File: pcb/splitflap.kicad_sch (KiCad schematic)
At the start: 61 parts, among them J1 Conn_01x05, J10 Hall C, J11 Hall-D, J12 I2C, J2 Conn_01x05, J3 Conn_01x05, J4 Conn_01x05, J5 Barrel_Jack_Switch, J6 USB_C_Receptacle_USB2.0_16P, J7 Barrel_Jack_Switch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

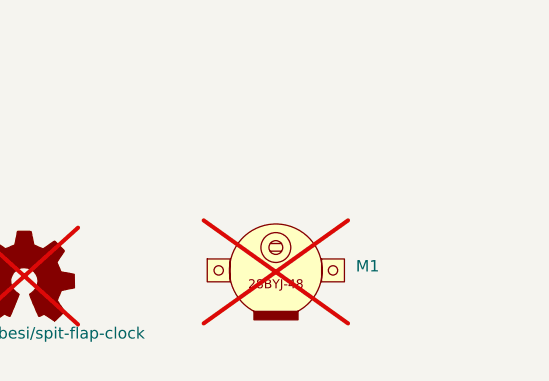
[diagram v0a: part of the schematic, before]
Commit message: Silkscreen improvements
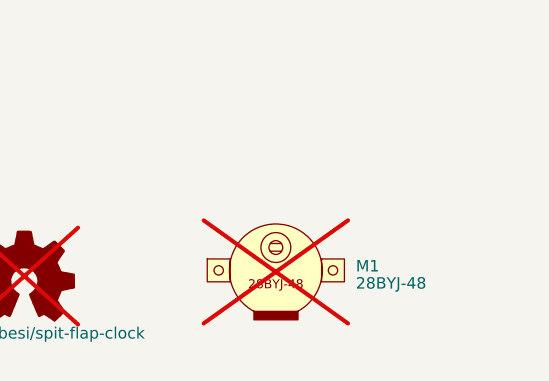
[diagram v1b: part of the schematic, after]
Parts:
- M1: value ~ -> 28BYJ-48
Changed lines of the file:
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@@
 			)
 		)
-		(property "Value" "~"
+		(property "Value" "28BYJ-48"
 			(at 269.24 174.1571 0)
 			(effects

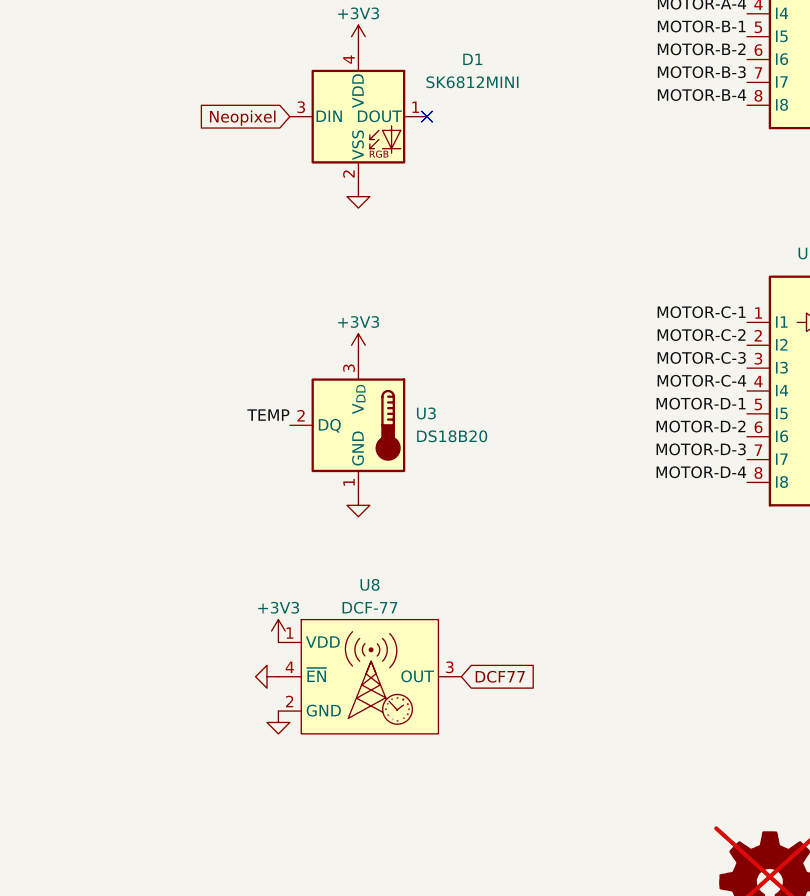
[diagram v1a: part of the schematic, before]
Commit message: Add optional LED for DCF receiver
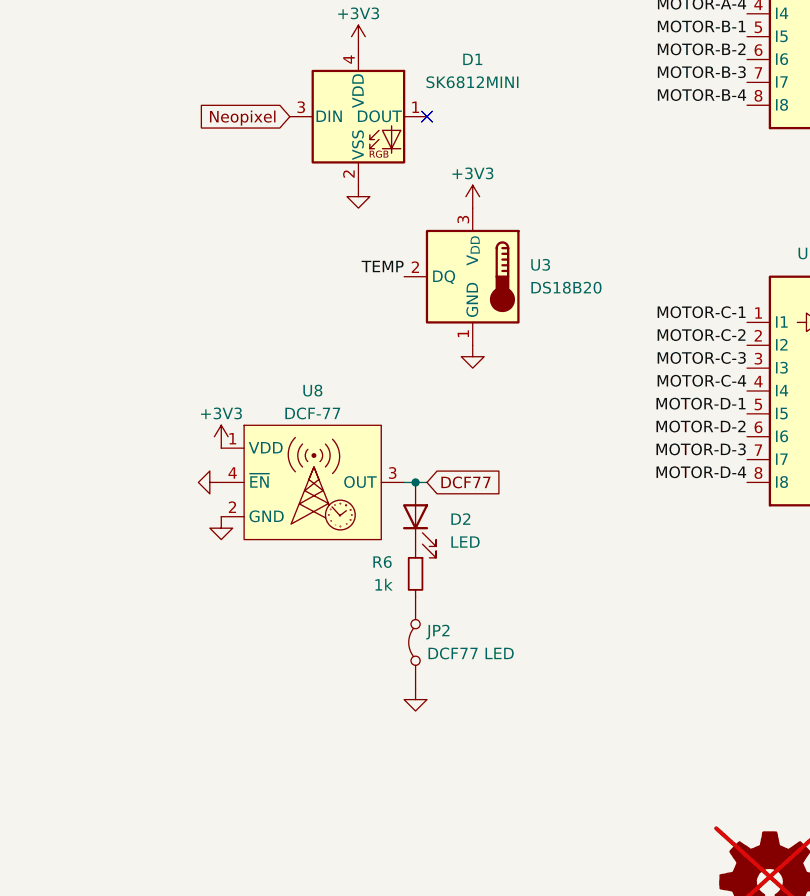
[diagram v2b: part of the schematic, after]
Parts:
- added D2: LED, LED_SMD:LED_0603_1608Metric_Pad1.05x0.95mm_HandSolder, symbol Device:LED
- added JP2: DCF77 LED, Jumper:SolderJumper-2_P1.3mm_Bridged_RoundedPad1.0x1.5mm, symbol Jumper:Jumper_2_Bridged
- added R6: 1k, Resistor_SMD:R_0603_1608Metric, symbol Device:R_Small
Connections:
- net DCF77: now also D2.2 (A)
- net GND: now also JP2.1 (A)
- new net: D2.1 (K), R6.1
- new net: JP2.2 (B), R6.2
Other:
- moved on the sheet: U3, U8

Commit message: Add two Hall sensors to the current board so that the amount of backlash can be registered
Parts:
- removed JP1: Hall-A Switch, Jumper:SolderJumper-3_P1.3mm_Open_RoundedPad1.0x1.5mm, symbol Jumper:Jumper_3_Bridged12
- removed TP1: IO7, TestPoint:TestPoint_Pad_D1.5mm, symbol Connector:TestPoint
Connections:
- net Extra is gone; now on net HALL_A2: U4.7 (IO7)
- net HALL_A is gone; now on net HALL_A1: J8.2 (Pin_2), U4.11 (IO18)
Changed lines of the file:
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@@
 		)
 	)
-	(label "HALL_A"
+	(label "HALL_A1"
 		(at 34.29 77.47 0)
 		(effects
@@
 	)
 	(label "HALL_A1"
-		(at 158.75 19.05 180)
+		(at 133.35 129.54 0)
 		(effects
 			(font
 				(size 1.27 1.27)
 			)
-			(justify right bottom)
+			(justify left bottom)
 		)
 	)
@@
 	)
 	(label "HALL_A2"
-		(at 171.45 19.05 0)
+		(at 133.35 101.6 0)
 		(effects
 			(font
@@
 		)
 	)
-	(label "HALL_A"
-		(at 165.1 22.86 270)
-		(effects
-			(font
-				(size 1.27 1.27)
-			)
-			(justify right bottom)
-		)
-	)
 	(label "SWA_SCL"
 		(at 133.35 127 0)
@@
 		)
 	)
-	(label "HALL_A"
-		(at 133.35 129.54 0)
-		(effects
-			(font
-				(size 1.27 1.27)
-			)
-			(justify left bottom)
-		)
-	)
 	(label "MOUT-A3"
 		(at 267.97 74.93 180)
@@
 		)
 	)
-	(global_label "Extra"
-		(shape input)
-		(at 133.35 101.6 0)
-		(fields_autoplaced yes)
-		(effects
-			(font
-				(size 1.27 1.27)
-			)
-			(justify left)
-		)
-		(property "Intersheetrefs" "${INTERSHEET_REFS}"
-			(at 141.1732 101.6 0)
-			(effects
-				(font
-					(size 1.27 1.27)
-				)
-				(justify left)
-				(hide yes)
-			)
-		)
-	)
 	(global_label "Neopixel"
 		(shape input)
@@
 		)
 	)
-	(global_label "Extra"
-		(shape input)
-		(at 175.26 67.31 180)
-		(fields_autoplaced yes)
-		(effects
-			(font
-				(size 1.27 1.27)
-			)
-			(justify right)
-		)
-		(property "Intersheetrefs" "${INTERSHEET_REFS}"
-			(at 167.4368 67.31 0)
-			(effects
-				(font
-					(size 1.27 1.27)
-				)
-				(justify right)
-				(hide yes)
-			)
-		)
-	)
 	(global_label "DCF77"
 		(shape input)
@@
 	)
 	(symbol
-		(lib_id "Jumper:Jumper_3_Bridged12")
-		(at 165.1 19.05 0)
-		(unit 1)
-		(exclude_from_sim yes)
-		(in_bom no)
-		(on_board yes)
-		(dnp no)
-		(fields_autoplaced yes)
-		(property "Reference" "JP1"
-			(at 165.1 12.7 0)
-			(effects
-				(font
-					(size 1.27 1.27)
-				)
-			)
-		)
-		(property "Value" "Hall-A Switch"
-			(at 165.1 15.24 0)
-			(effects
-				(font
-					(size 1.27 1.27)
-				)
-			)
-		)
-		(property "Footprint" "Jumper:SolderJumper-3_P1.3mm_Open_RoundedPad1.0x1.5mm"
-			(at 165.1 19.05 0)
-			(effects
-				(font
-					(size 1.27 1.27)
-				)
-				(hide yes)
-			)
-		)
-		(property "Datasheet" "~"
-			(at 165.1 19.05 0)
-			(effects
-				(font
-					(size 1.27 1.27)
-				)
-				(hide yes)
-			)
-		)
-		(property "Description" "Jumper, 3-pole, pins 1+2 closed/bridged"
-			(at 165.1 19.05 0)
-			(effects
-				(font
-					(size 1.27 1.27)
-				)
-				(hide yes)
-			)
-		)
-		(pin "1"
-		)
-		(pin "3"
-		)
-		(pin "2"
-		)
-		(instances
-			(project ""
-				(path "/f3b5a3df-7272-4af1-9be6-6c38555ab067"
-					(reference "JP1")
-					(unit 1)
-				)
-			)
-		)
-	)
-	(symbol
 		(lib_id "power:GND")
 		(at 36.83 97.79 0)
@@
 					(unit 1)
 				)
-			)
-		)
-	)
-	(symbol
-		(lib_id "Connector:TestPoint")
-		(at 175.26 67.31 270)
-		(unit 1)
-		(exclude_from_sim no)
-		(in_bom yes)
-		(on_board yes)
-		(dnp no)
-		(fields_autoplaced yes)
-		(property "Reference" "TP1"
-			(at 180.34 66.0399 90)
-			(effects
-				(font
-					(size 1.27 1.27)
-				)
-				(justify left)
-			)
-		)
-		(property "Value" "IO7"
-			(at 180.34 68.5799 90)
-			(effects
-				(font
-					(size 1.27 1.27)
-				)
-				(justify left)
-			)
-		)
-		(property "Footprint" "TestPoint:TestPoint_Pad_D1.5mm"
-			(at 175.26 72.39 0)
-			(effects
-				(font
-					(size 1.27 1.27)
-				)
-				(hide yes)
-			)
-		)
-		(property "Datasheet" "~"
-			(at 175.26 72.39 0)
-			(effects
-				(font
-					(size 1.27 1.27)
-				)
-				(hide yes)
-			)
-		)
-		(property "Description" "test point"
-			(at 175.26 67.31 0)
-			(effects
-				(font
-					(size 1.27 1.27)
-				)
-				(hide yes)
-			)
-		)
-		(pin "1"
-		)
-		(instances
-			(project ""
-				(path "/f3b5a3df-7272-4af1-9be6-6c38555ab067"
-					(reference "TP1")
-					(unit 1)
-				)

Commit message: Remapping the motors ABCD to match the connectors on the board
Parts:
- J1: value Conn_01x05 -> Motor D
- J11: value Hall-D -> Hall B
- J2: value Conn_01x05 -> Motor C
- J3: value Conn_01x05 -> Motor B
- J4: value Conn_01x05 -> Motor A
- J8: value Hall A -> Hall A1
- J9: value Hall B -> Hall D
- U5: value AH1815-W-7 -> Hall A1; MPN (none) -> AH1815-W-7
- U9: value AH1815-W-7 -> Hall A2; MPN (none) -> AH1815-W-7
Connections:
- net HALL_B: now also J11.2 (Pin_2), U4.20 (IO12); no longer J9.2 (Pin_2), U4.25 (IO48)
- net HALL_D: now also J9.2 (Pin_2), U4.25 (IO48); no longer J11.2 (Pin_2), U4.20 (IO12)
- net MOTOR-A-1: now also U2.5 (I5), U4.18 (IO10); no longer U1.1 (I1), U4.39 (IO1)
- net MOTOR-A-2: now also U2.6 (I6), U4.17 (IO9); no longer U1.2 (I2), U4.38 (IO2)
- net MOTOR-A-3: now also U2.7 (I7), U4.15 (IO3); no longer U1.3 (I3), U4.35 (MTMS/IO42)
- net MOTOR-A-4: now also U2.8 (I8), U4.12 (IO8); no longer U1.4 (I4), U4.34 (MTDI/IO41)
- net MOTOR-B-1: now also U2.1 (I1), U4.21 (IO13); no longer U1.5 (I5), U4.33 (MTDO/IO40)
- net MOTOR-B-2: now also U2.2 (I2), U4.22 (IO14); no longer U1.6 (I6), U4.32 (MTCK/IO39)
- net MOTOR-B-3: now also U2.3 (I3), U4.23 (IO21); no longer U1.7 (I7), U4.31 (IO38)
- net MOTOR-B-4: now also U2.4 (I4), U4.19 (IO11); no longer U1.8 (I8), U4.6 (IO6)
- net MOTOR-C-1: now also U1.5 (I5), U4.33 (MTDO/IO40); no longer U2.1 (I1), U4.21 (IO13)
- net MOTOR-C-2: now also U1.6 (I6), U4.32 (MTCK/IO39); no longer U2.2 (I2), U4.22 (IO14)
- net MOTOR-C-3: now also U1.7 (I7), U4.31 (IO38); no longer U2.3 (I3), U4.23 (IO21)
- net MOTOR-C-4: now also U1.8 (I8), U4.6 (IO6); no longer U2.4 (I4), U4.19 (IO11)
- net MOTOR-D-1: now also U1.1 (I1), U4.39 (IO1); no longer U2.5 (I5), U4.18 (IO10)
- net MOTOR-D-2: now also U1.2 (I2), U4.38 (IO2); no longer U2.6 (I6), U4.17 (IO9)
- net MOTOR-D-3: now also U1.3 (I3), U4.35 (MTMS/IO42); no longer U2.7 (I7), U4.15 (IO3)
- net MOTOR-D-4: now also U1.4 (I4), U4.34 (MTDI/IO41); no longer U2.8 (I8), U4.12 (IO8)
- net MOUT-A1: now also J4.1 (Pin_1), U2.14 (O5); no longer J1.1 (Pin_1), U1.18 (O1)
- net MOUT-A2: now also J4.2 (Pin_2), U2.13 (O6); no longer J1.2 (Pin_2), U1.17 (O2)
- net MOUT-A3: now also J4.3 (Pin_3), U2.12 (O7); no longer J1.3 (Pin_3), U1.16 (O3)
- net MOUT-A4: now also J4.4 (Pin_4), U2.11 (O8); no longer J1.4 (Pin_4), U1.15 (O4)
- net MOUT-B1: now also J3.1 (Pin_1), U2.18 (O1); no longer J2.1 (Pin_1), U1.14 (O5)
- net MOUT-B2: now also J3.2 (Pin_2), U2.17 (O2); no longer J2.2 (Pin_2), U1.13 (O6)
- net MOUT-B3: now also J3.3 (Pin_3), U2.16 (O3); no longer J2.3 (Pin_3), U1.12 (O7)
- net MOUT-B4: now also J3.4 (Pin_4), U2.15 (O4); no longer J2.4 (Pin_4), U1.11 (O8)
- net MOUT-C1: now also J2.1 (Pin_1), U1.14 (O5); no longer J3.1 (Pin_1), U2.18 (O1)
- net MOUT-C2: now also J2.2 (Pin_2), U1.13 (O6); no longer J3.2 (Pin_2), U2.17 (O2)
- net MOUT-C3: now also J2.3 (Pin_3), U1.12 (O7); no longer J3.3 (Pin_3), U2.16 (O3)
- net MOUT-C4: now also J2.4 (Pin_4), U1.11 (O8); no longer J3.4 (Pin_4), U2.15 (O4)
- net MOUT-D1: now also J1.1 (Pin_1), U1.18 (O1); no longer J4.1 (Pin_1), U2.14 (O5)
- net MOUT-D2: now also J1.2 (Pin_2), U1.17 (O2); no longer J4.2 (Pin_2), U2.13 (O6)
- net MOUT-D3: now also J1.3 (Pin_3), U1.16 (O3); no longer J4.3 (Pin_3), U2.12 (O7)
- net MOUT-D4: now also J1.4 (Pin_4), U1.15 (O4); no longer J4.4 (Pin_4), U2.11 (O8)
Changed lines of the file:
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@@
 		)
 	)
-	(label "MOTOR-B-1"
+	(label "MOTOR-C-1"
 		(at 229.87 80.01 180)
 		(effects
@@
 	)
 	(label "MOUT-B3"
-		(at 267.97 88.9 180)
+		(at 267.97 116.84 180)
 		(effects
 			(font
@@
 		)
 	)
-	(label "MOUT-A2"
+	(label "MOUT-D2"
 		(at 267.97 72.39 180)
 		(effects
@@
 		)
 	)
-	(label "MOTOR-B-2"
+	(label "MOTOR-C-2"
 		(at 229.87 82.55 180)
 		(effects
@@
 		)
 	)
-	(label "MOTOR-B-1"
+	(label "MOTOR-C-1"
 		(at 133.35 144.78 0)
 		(effects
@@
 		)
 	)
-	(label "MOTOR-D-2"
+	(label "MOTOR-A-2"
 		(at 229.87 124.46 180)
 		(effects
@@
 		)
 	)
-	(label "MOTOR-C-3"
+	(label "MOTOR-B-3"
 		(at 133.35 137.16 0)
 		(effects
@@
 		)
 	)
-	(label "MOTOR-D-1"
+	(label "MOTOR-A-1"
 		(at 229.87 121.92 180)
 		(effects
@@
 		)
 	)
-	(label "MOTOR-D-3"
+	(label "MOTOR-A-3"
 		(at 229.87 127 180)
 		(effects
@@
 		)
 	)
-	(label "MOTOR-D-1"
+	(label "MOTOR-A-1"
 		(at 133.35 109.22 0)
 		(effects
@@
 		)
 	)
-	(label "MOTOR-B-4"
+	(label "MOTOR-C-4"
 		(at 133.35 99.06 0)
 		(effects
@@
 		)
 	)
-	(label "MOTOR-B-4"
+	(label "MOTOR-C-4"
 		(at 229.87 87.63 180)
 		(effects
@@
 		)
 	)
-	(label "MOTOR-D-2"
+	(label "MOTOR-A-2"
 		(at 133.35 106.68 0)
 		(effects
@@
 	)
 	(label "MOUT-B2"
-		(at 267.97 86.36 180)
+		(at 267.97 114.3 180)
 		(effects
 			(font
@@
 		)
 	)
-	(label "MOTOR-A-2"
+	(label "MOTOR-D-2"
 		(at 229.87 72.39 180)
 		(effects
@@
 		)
 	)
-	(label "MOUT-A1"
+	(label "MOUT-D1"
 		(at 267.97 69.85 180)
 		(effects
@@
 		)
 	)
-	(label "MOTOR-B-3"
+	(label "MOTOR-C-3"
 		(at 133.35 139.7 0)
 		(effects
@@
 		)
 	)
-	(label "MOTOR-A-3"
+	(label "MOTOR-D-3"
 		(at 229.87 74.93 180)
 		(effects
@@
 		)
 	)
-	(label "MOTOR-A-1"
+	(label "MOTOR-D-1"
 		(at 133.35 86.36 0)
 		(effects
@@
 	)
 	(label "MOUT-C3"
-		(at 267.97 116.84 180)
+		(at 267.97 88.9 180)
 		(effects
 			(font
@@
 		)
 	)
-	(label "MOTOR-B-3"
+	(label "MOTOR-C-3"
 		(at 229.87 85.09 180)
 		(effects
@@
 	)
 	(label "MOUT-B1"
-		(at 267.97 83.82 180)
+		(at 267.97 111.76 180)
 		(effects
 			(font
@@
 		)
 	)
-	(label "MOUT-A4"
+	(label "MOUT-D4"
 		(at 267.97 77.47 180)
 		(effects
@@
 		)
 	)
-	(label "HALL_B"
+	(label "HALL_D"
 		(at 34.29 95.25 0)
 		(effects
@@
 		)
 	)
-	(label "MOTOR-C-3"
+	(label "MOTOR-B-3"
 		(at 229.87 116.84 180)
 		(effects
@@
 		)
 	)
-	(label "MOTOR-C-2"
+	(label "MOTOR-B-2"
 		(at 133.35 119.38 0)
 		(effects
@@
 		)
 	)
-	(label "MOTOR-C-1"
+	(label "MOTOR-B-1"
 		(at 229.87 111.76 180)
 		(effects
@@
 		)
 	)
-	(label "HALL_D"
+	(label "HALL_B"
 		(at 133.35 114.3 0)
 		(effects
@@
 		)
 	)
-	(label "MOTOR-C-4"
+	(label "MOTOR-B-4"
 		(at 133.35 111.76 0)
 		(effects
@@
 		)
 	)
-	(label "MOTOR-D-4"
+	(label "MOTOR-A-4"
 		(at 133.35 104.14 0)
 		(effects
@@
 		)
 	)
-	(label "MOTOR-C-1"
+	(label "MOTOR-B-1"
 		(at 133.35 116.84 0)
 		(effects
@@
 		)
 	)
-	(label "MOUT-D2"
+	(label "MOUT-A2"
 		(at 267.97 130.81 180)
 		(effects
@@
 		)
 	)
-	(label "MOTOR-A-2"
+	(label "MOTOR-D-2"
 		(at 133.35 88.9 0)
 		(effects
@@
 		)
 	)
-	(label "MOTOR-C-4"
+	(label "MOTOR-B-4"
 		(at 229.87 119.38 180)
 		(effects
@@
 		)
 	)
-	(label "MOTOR-D-3"
+	(label "MOTOR-A-3"
 		(at 133.35 91.44 0)
 		(effects
@@
 		)
 	)
-	(label "HALL_D"
+	(label "HALL_B"
 		(at 34.29 130.81 0)
 		(effects
@@
 		)
 	)
-	(label "MOTOR-A-4"
+	(label "MOTOR-D-4"
 		(at 229.87 77.47 180)
 		(effects
@@
 		)
 	)
-	(label "MOTOR-A-1"
+	(label "MOTOR-D-1"
 		(at 229.87 69.85 180)
 		(effects
@@
 		)
 	)
-	(label "MOTOR-B-2"
+	(label "MOTOR-C-2"
 		(at 133.35 142.24 0)
 		(effects
@@
 		)
 	)
-	(label "MOUT-D1"
+	(label "MOUT-A1"
 		(at 267.97 128.27 180)
 		(effects
@@
 	)
 	(label "MOUT-C2"
-		(at 267.97 114.3 180)
+		(at 267.97 86.36 180)
 		(effects
 			(font
@@
 	)
 	(label "MOUT-C1"
-		(at 267.97 111.76 180)
+		(at 267.97 83.82 180)
 		(effects
 			(font
@@
 		)
 	)
-	(label "MOTOR-A-3"
+	(label "MOTOR-D-3"
 		(at 133.35 149.86 0)
 		(effects
@@
 		)
 	)
-	(label "MOTOR-D-4"
+	(label "MOTOR-A-4"
 		(at 229.87 129.54 180)
 		(effects
@@
 	)
 	(label "MOUT-C4"
-		(at 267.97 119.38 180)
+		(at 267.97 91.44 180)
 		(effects
 			(font
@@
 	)
 	(label "MOUT-B4"
-		(at 267.97 91.44 180)
+		(at 267.97 119.38 180)
 		(effects
 			(font
@@
 		)
 	)
-	(label "MOUT-D3"
+	(label "MOUT-A3"
 		(at 267.97 133.35 180)
 		(effects
@@
 		)
 	)
-	(label "MOUT-D4"
+	(label "MOUT-A4"
 		(at 267.97 135.89 180)
 		(effects
@@
 		)
 	)
-	(label "HALL_B"
+	(label "HALL_D"
 		(at 133.35 165.1 0)
 		(effects
@@
 		)
 	)
-	(label "MOUT-A3"
+	(label "MOUT-D3"
 		(at 267.97 74.93 180)
 		(effects
@@
 		)
 	)
-	(label "MOTOR-A-4"
+	(label "MOTOR-D-4"
 		(at 133.35 147.32 0)
 		(effects
@@
 		)
 	)
-	(label "MOTOR-C-2"
+	(label "MOTOR-B-2"
 		(at 229.87 114.3 180)
 		(effects
@@
 			)
 		)
-		(property "Value" "AH1815-W-7"
+		(property "Value" "Hall A1"
 			(at 250.19 30.48 0)
 			(effects
@@
 			)
 		)
-		(property "MPN" " "
+		(property "MPN" "AH1815-W-7"
 			(at 243.84 31.75 0)
 			(effects
@@
 			)
 		)
-		(property "Value" "Hall-D"
+		(property "Value" "Hall B"
 			(at 29.21 125.095 0)
 			(effects
@@
 			)
 		)
-		(property "Value" "Hall A"
+		(property "Value" "Hall A1"
 			(at 29.21 71.12 0)
 			(effects
@@
 			)
 		)
-		(property "Value" "AH1815-W-7"
+		(property "Value" "Hall A2"
 			(at 250.19 5.08 0)
 			(effects
@@
 			)
 		)
-		(property "MPN" " "
+		(property "MPN" "AH1815-W-7"
 			(at 243.84 6.35 0)
 			(effects
@@
 			)
 		)
-		(property "Value" "Conn_01x05"
+		(property "Value" "Motor D"
 			(at 275.59 76.1999 0)
 			(effects
@@
 			)
 		)
-		(property "Value" "Conn_01x05"
+		(property "Value" "Motor C"
 			(at 275.59 90.1699 0)
 			(effects
@@
 			)
 		)
-		(property "Value" "Conn_01x05"
+		(property "Value" "Motor A"
 			(at 275.59 134.6199 0)
 			(effects
@@
 			)
 		)
-		(property "Value" "Hall B"
+		(property "Value" "Hall D"
 			(at 29.21 89.535 0)
 			(effects
@@
 			)
 		)
-		(property "Value" "Conn_01x05"
+		(property "Value" "Motor B"
 			(at 275.59 118.1099 0)
 			(effects

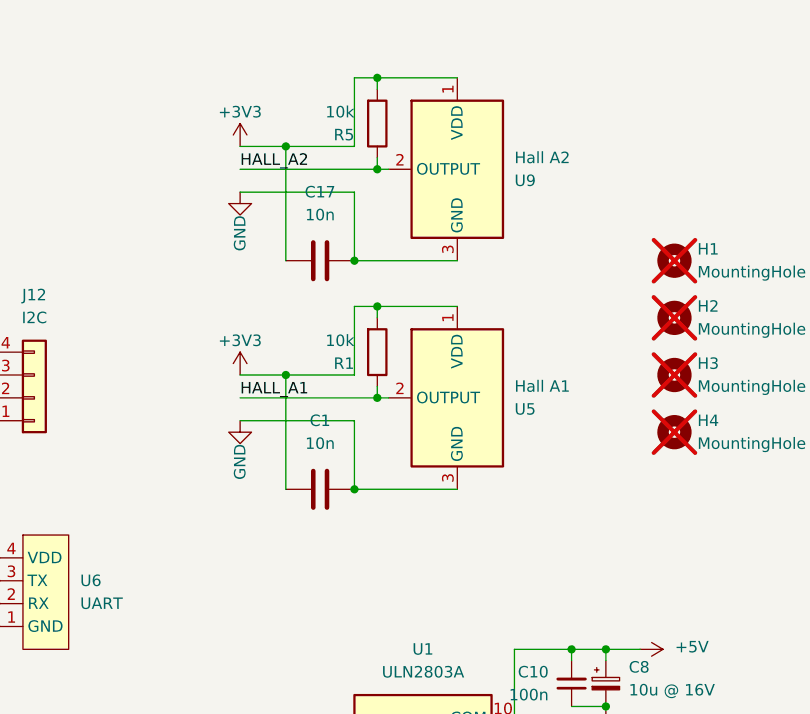
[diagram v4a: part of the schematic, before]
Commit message: Add capacitors for hall sensors power pins
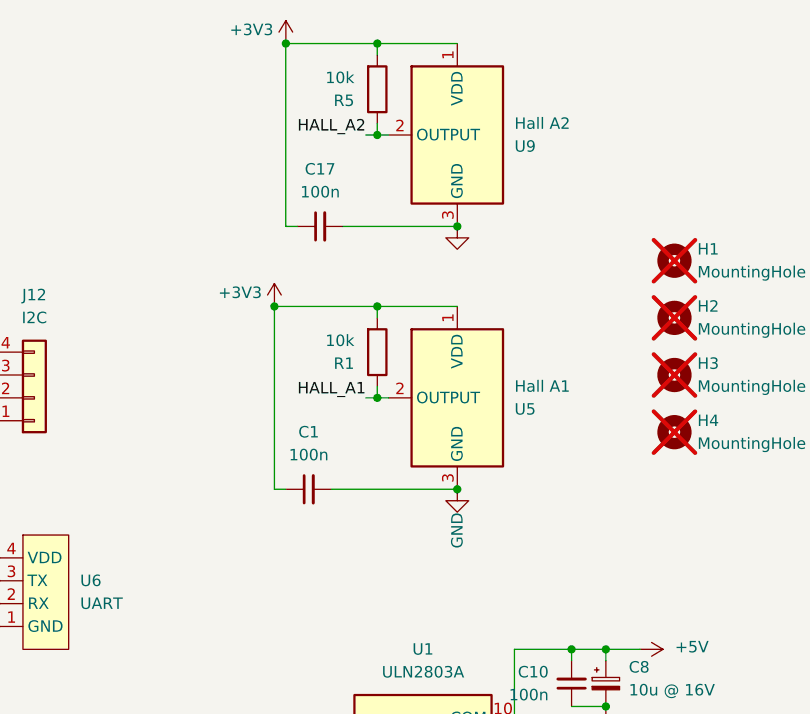
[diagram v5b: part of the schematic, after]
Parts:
- removed C1, C17: 10n, symbol Device:C
- added C1, C17: 100n, Capacitor_SMD:C_0805_2012Metric_Pad1.18x1.45mm_HandSolder, symbol Device:C_Small
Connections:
- net +3V3: now also C1.1, C17.1
- net GND: now also C1.2, C17.2
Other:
- moved on the sheet: R5, U9
